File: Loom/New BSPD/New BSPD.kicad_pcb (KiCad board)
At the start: 2 copper layers, 148.6 x 83.8 mm, 62 parts, among them J1 Conn_01x03, J2 Conn_01x03, J3 Conn_01x03, J4 Screw_Terminal_01x02, K1 MCCMA51-S-DC12V-C, Q1 IRLZ44Z, U1 4011, U10 LM2901, U11 4012, U12 74LS573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

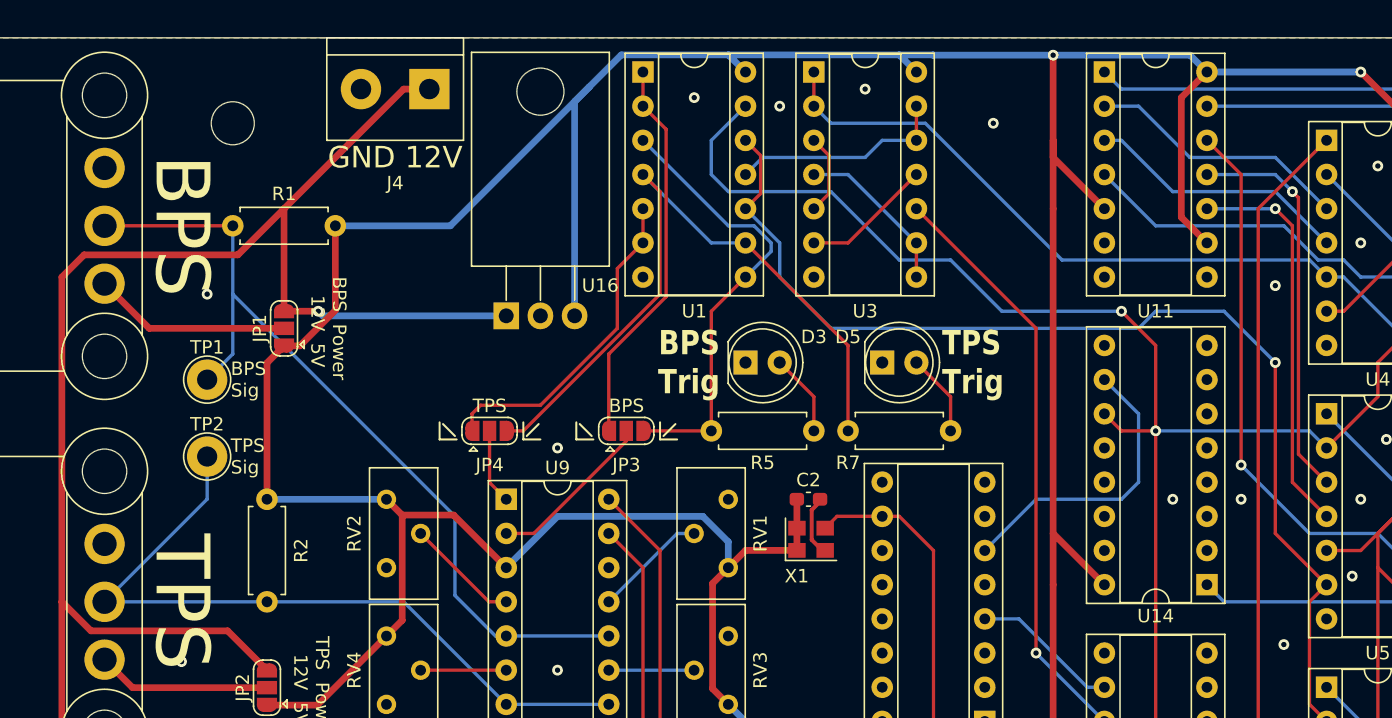
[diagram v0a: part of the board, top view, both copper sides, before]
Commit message: Change BSPD Power connector
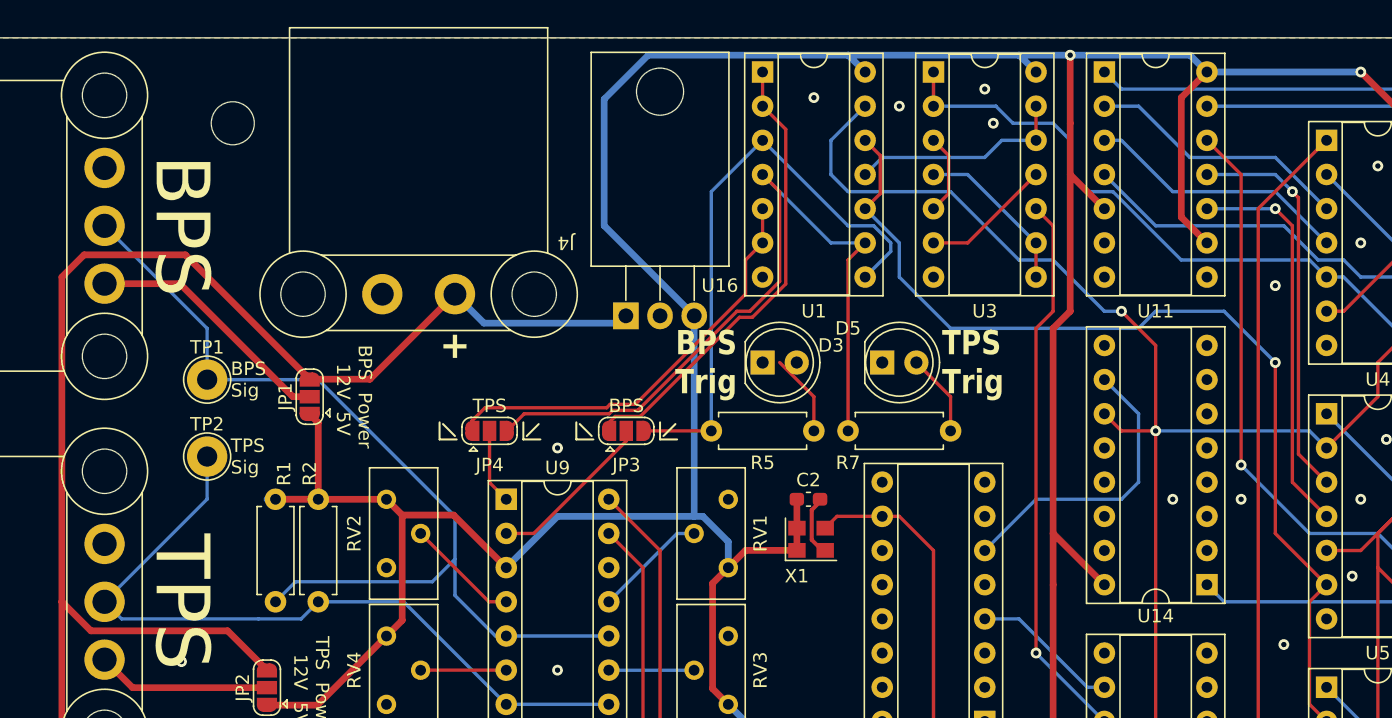
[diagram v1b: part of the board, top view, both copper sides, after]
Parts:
- J4: footprint TerminalBlock:TerminalBlock_bornier-2_P5.08mm -> BSPD_footprints:ATF13-2P-BM03
- moved R1 28.1 mm to (84.5, 64.8), turned to 90 degrees
- moved J4 15.4 mm to (97.8, 41.9)
- moved U1 8.89 mm to (120.7, 25.4)
- moved U16 8.89 mm to (110.5, 43.5)
- moved U3 8.89 mm to (133.3, 25.4)
- moved JP1 5.43 mm to (87.0, 49.5)
- moved R2 3.81 mm to (87.6, 64.8)
- moved D3 1.27 mm to (120.7, 47.0)
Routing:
- net +5V: track 475.2 -> 447.9 mm
- net /BPS_Trig: track 33.5 -> 44.2 mm
- net /System_OK: track 82.0 -> 73.1 mm
- net /State Machine/State_B: track 230.8 -> 221.9 mm
- net Net-(JP4-A): track 24.4 -> 31.8 mm
- net /SM_Ok: track 205.2 -> 197.8 mm
- net +12V: track 153.5 -> 146.3 mm, vias 1 -> 0
- net /BPS_Sig: track 63.7 -> 70.4 mm
- net /TPS_Trig: track 51.8 -> 57.5 mm
- net Net-(JP3-A): track 29.1 -> 34.5 mm
- net /BPS_Power: track 14.7 -> 18.7 mm
- net /State Machine/Timers/Reset_Counting: track 43.9 -> 41.3 mm
- net /TPS_Sig: track 54.6 -> 55.6 mm
- net GND: vias 24 -> 23
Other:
- board text added: "+"
- board text added: "12V GND"
- board text removed: "GND 12V"

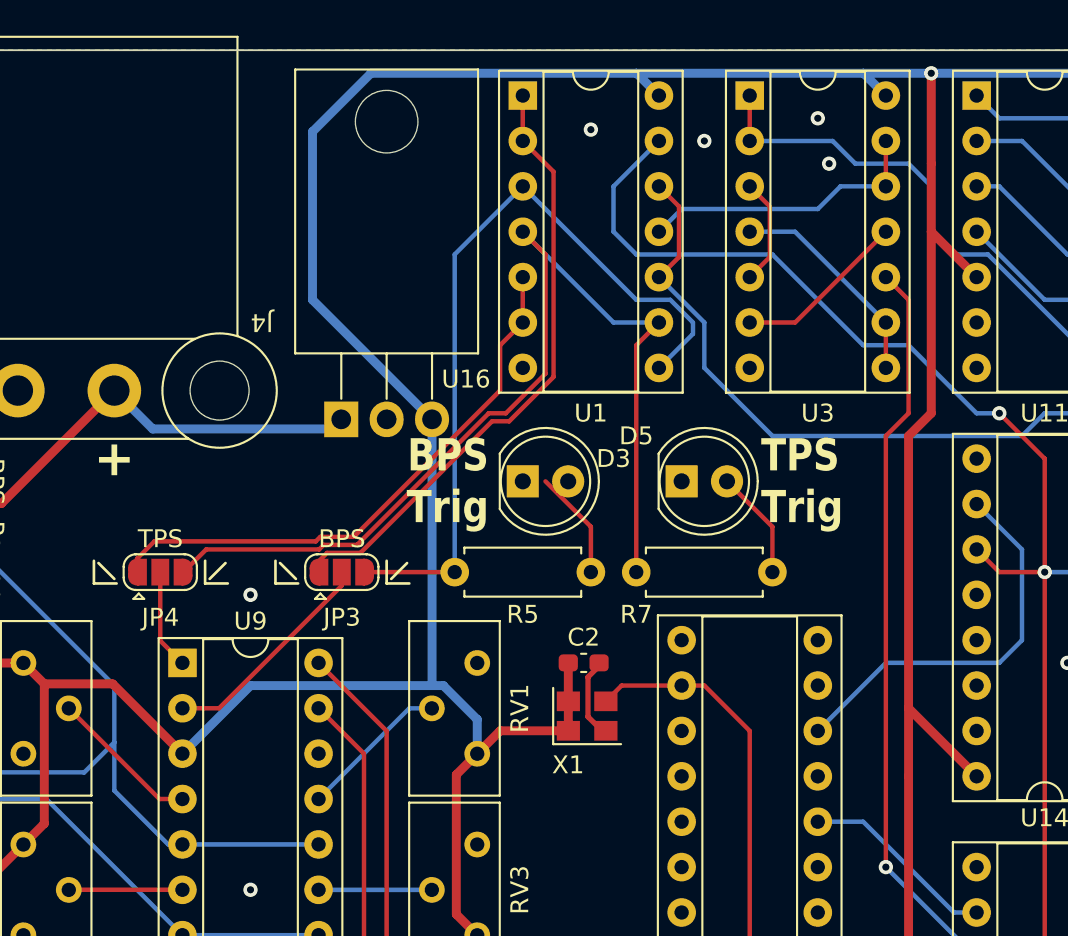
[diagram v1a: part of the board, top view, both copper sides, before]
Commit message: Minor changes to pass DRC
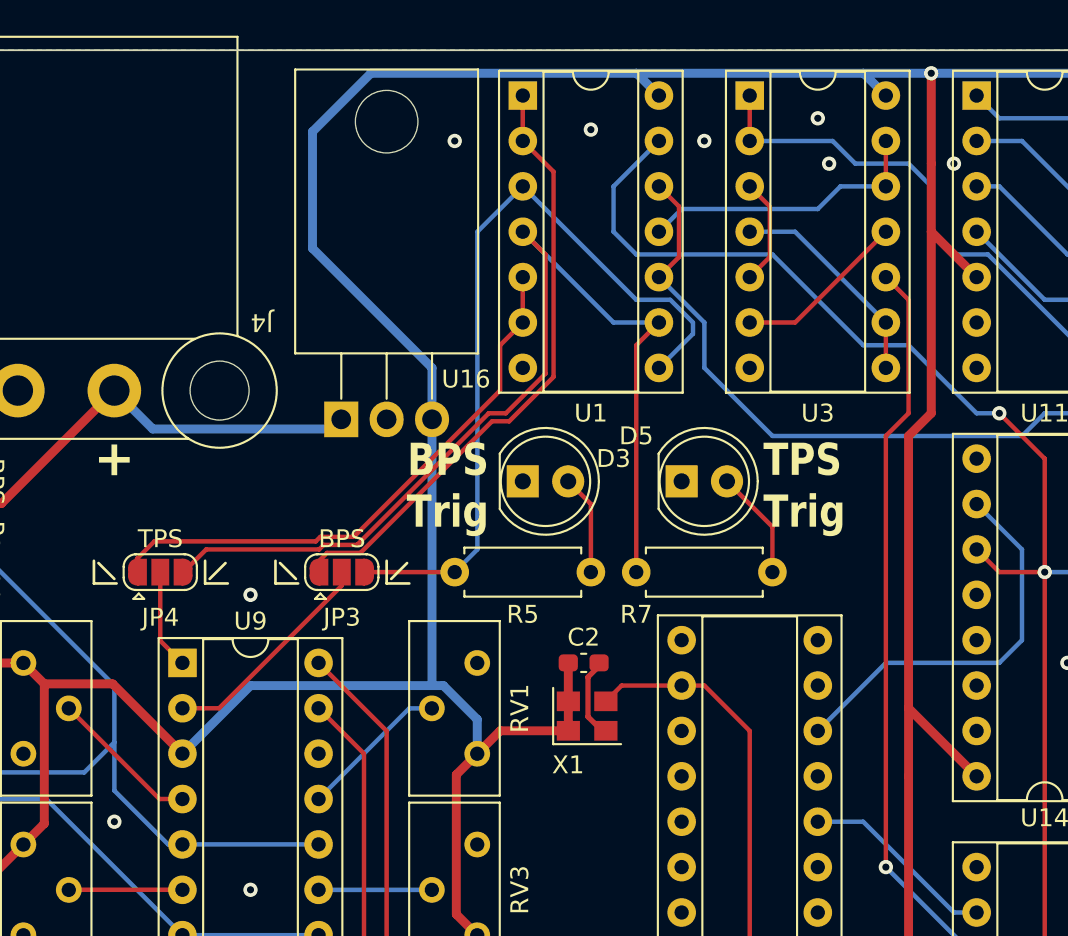
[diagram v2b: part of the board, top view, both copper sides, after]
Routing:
- net Net-(D3-A): track 6.13 -> 5.61 mm
- net GND: vias 23 -> 26
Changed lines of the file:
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@@
     (effects (font (size 1 1) (thickness 0.15)) (justify left))
   )
-  (gr_text "TPS\nTrig" (at 133.985 46.99) (layer "F.SilkS")
+  (gr_text "TPS\nTrig" (at 134.112 47.244) (layer "F.SilkS")
     (effects (font (size 1.8 1.5) (thickness 0.3) bold) (justify left))
   )
@@
     (effects (font (size 2 2) (thickness 0.4) bold))
   )
-  (gr_text "BPS\nTrig" (at 118.745 46.99) (layer "F.SilkS")
+  (gr_text "BPS\nTrig" (at 118.745 47.244) (layer "F.SilkS")
     (effects (font (size 1.8 1.5) (thickness 0.3) bold) (justify right))
   )
@@
   (segment (start 139.72 24.15) (end 139.7 24.15) (width 0.5) (layer "B.Cu") (net 1))
   (segment (start 116.205 58.42) (end 115.57 58.42) (width 0.5) (layer "B.Cu") (net 1))
-  (segment (start 108.88 27.419009) (end 108.88 36.83) (width 0.5) (layer "B.Cu") (net 1))
   (segment (start 115.57 43.52) (end 115.57 58.42) (width 0.5) (layer "B.Cu") (net 1))
   (segment (start 118.1 62.235) (end 118.1 60.315) (width 0.5) (layer "B.Cu") (net 1))
@@
   (segment (start 128.27 25.4) (end 127.02 24.15) (width 0.5) (layer "B.Cu") (net 1))
   (segment (start 184.235 59.605) (end 186.68 59.605) (width 0.5) (layer "B.Cu") (net 1))
+  (segment (start 112.149009 24.15) (end 127 24.15) (width 0.5) (layer "B.Cu") (net 1))
   (segment (start 186.68 59.605) (end 187.875 59.605) (width 0.5) (layer "B.Cu") (net 1))
   (segment (start 127.02 24.15) (end 127 24.15) (width 0.5) (layer "B.Cu") (net 1))
@@
   (segment (start 181.695 41.825) (end 184.235 39.285) (width 0.5) (layer "B.Cu") (net 1))
   (segment (start 195.58 74.85) (end 194.31 76.12) (width 0.5) (layer "B.Cu") (net 1))
+  (segment (start 115.57 40.64) (end 108.88 33.95) (width 0.5) (layer "B.Cu") (net 1))
   (segment (start 118.1 60.315) (end 116.205 58.42) (width 0.5) (layer "B.Cu") (net 1))
   (segment (start 119.365 73.66) (end 118.1 72.395) (width 0.5) (layer "B.Cu") (net 1))
@@
   (segment (start 139.7 24.15) (end 127 24.15) (width 0.5) (layer "B.Cu") (net 1))
   (segment (start 105.41 58.42) (end 101.6 62.23) (width 0.5) (layer "B.Cu") (net 1))
-  (segment (start 127 24.15) (end 112.149009 24.15) (width 0.5) (layer "B.Cu") (net 1))
   (segment (start 140.97 25.4) (end 139.72 24.15) (width 0.5) (layer "B.Cu") (net 1))
   (segment (start 196.77 81.2) (end 196.85 81.28) (width 0.5) (layer "B.Cu") (net 1))
-  (segment (start 115.57 43.52) (end 108.88 36.83) (width 0.5) (layer "B.Cu") (net 1))
   (segment (start 187.875 59.605) (end 195.58 67.31) (width 0.5) (layer "B.Cu") (net 1))
   (segment (start 196.85 76.12) (end 196.85 81.28) (width 0.5) (layer "B.Cu") (net 1))
@@
   (segment (start 195.58 67.31) (end 195.58 74.85) (width 0.5) (layer "B.Cu") (net 1))
   (segment (start 179.06 41.825) (end 181.695 41.825) (width 0.5) (layer "B.Cu") (net 1))
-  (segment (start 112.149009 24.15) (end 108.88 27.419009) (width 0.5) (layer "B.Cu") (net 1))
   (segment (start 153.67 25.4) (end 165.1 25.4) (width 0.5) (layer "B.Cu") (net 1))
   (segment (start 175.335 38.1) (end 175.26 38.1) (width 0.5) (layer "B.Cu") (net 1))
+  (segment (start 108.88 33.95) (end 108.88 27.419009) (width 0.5) (layer "B.Cu") (net 1))
   (segment (start 179.06 62.145) (end 181.695 62.145) (width 0.5) (layer "B.Cu") (net 1))
   (segment (start 129.54 73.66) (end 119.365 73.66) (width 0.5) (layer "B.Cu") (net 1))
   (segment (start 195.58 74.85) (end 196.85 76.12) (width 0.5) (layer "B.Cu") (net 1))
+  (segment (start 115.57 43.52) (end 115.57 40.64) (width 0.5) (layer "B.Cu") (net 1))
   (segment (start 179.06 41.825) (end 175.335 38.1) (width 0.5) (layer "B.Cu") (net 1))
   (segment (start 115.57 58.42) (end 105.41 58.42) (width 0.5) (layer "B.Cu") (net 1))
@@
   (segment (start 184.235 39.285) (end 186.68 39.285) (width 0.5) (layer "B.Cu") (net 1))
   (segment (start 181.695 62.145) (end 184.235 59.605) (width 0.5) (layer "B.Cu") (net 1))
+  (segment (start 108.88 27.419009) (end 112.149009 24.15) (width 0.5) (layer "B.Cu") (net 1))
   (segment (start 195.58 87.55) (end 196.85 86.28) (width 0.25) (layer "B.Cu") (net 2))
   (segment (start 191.77 87.55) (end 195.58 87.55) (width 0.25) (layer "B.Cu") (net 2))
@@
   (via (at 159.385 67.945) (size 0.8) (drill 0.4) (layers "F.Cu" "B.Cu") (free) (net 5))
   (via (at 164.465 62.865) (size 0.8) (drill 0.4) (layers "F.Cu" "B.Cu") (free) (net 5))
+  (via (at 116.84 27.94) (size 0.8) (drill 0.4) (layers "F.Cu" "B.Cu") (free) (net 5))
   (via (at 167.005 52.705) (size 0.8) (drill 0.4) (layers "F.Cu" "B.Cu") (free) (net 5))
   (via (at 128.27 96.52) (size 0.8) (drill 0.4) (layers "F.Cu" "B.Cu") (free) (net 5))
+  (via (at 144.78 29.21) (size 0.8) (drill 0.4) (layers "F.Cu" "B.Cu") (free) (net 5))
   (via (at 137.795 29.21) (size 0.8) (drill 0.4) (layers "F.Cu" "B.Cu") (free) (net 5))
   (via (at 137.16 26.67) (size 0.8) (drill 0.4) (layers "F.Cu" "B.Cu") (free) (net 5))
   (via (at 130.81 27.94) (size 0.8) (drill 0.4) (layers "F.Cu" "B.Cu") (free) (net 5))
   (via (at 105.41 69.85) (size 0.8) (drill 0.4) (layers "F.Cu" "B.Cu") (free) (net 5))
+  (via (at 97.79 66.04) (size 0.8) (drill 0.4) (layers "F.Cu" "B.Cu") (free) (net 5))
   (via (at 165.1 38.1) (size 0.8) (drill 0.4) (layers "F.Cu" "B.Cu") (free) (net 5))
   (segment (start 151.13 100.33) (end 151.13 102.87) (width 0.25) (layer "F.Cu") (net 6))
   (segment (start 148.59 97.79) (end 151.13 100.33) (width 0.25) (layer "F.Cu") (net 6))
-  (segment (start 124.46 49.53) (end 124.46 52.07) (width 0.25) (layer "F.Cu") (net 7))
-  (segment (start 121.92 46.99) (end 124.46 49.53) (width 0.25) (layer "F.Cu") (net 7))
+  (segment (start 124.46 48.26) (end 123.19 46.99) (width 0.25) (layer "F.Cu") (net 7))
+  (segment (start 124.46 52.07) (end 124.46 48.26) (width 0.25) (layer "F.Cu") (net 7))
   (segment (start 161.29 100.33) (end 161.29 102.87) (width 0.25) (layer "F.Cu") (net 8))
   (segment (start 158.75 97.79) (end 161.29 100.33) (width 0.25) (layer "F.Cu") (net 8))
@@
   (segment (start 120.65 30.48) (end 127 36.83) (width 0.25) (layer "B.Cu") (net 19))
   (segment (start 130.175 38.101396) (end 130.175 38.735) (width 0.25) (layer "B.Cu") (net 19))
-  (segment (start 116.84 34.29) (end 116.84 52.07) (width 0.25) (layer "B.Cu") (net 19))
+  (segment (start 120.65 30.48) (end 118.11 33.02) (width 0.25) (layer "B.Cu") (net 19))
+  (segment (start 118.11 50.8) (end 116.84 52.07) (width 0.25) (layer "B.Cu") (net 19))
   (segment (start 130.175 38.735) (end 128.27 40.64) (width 0.25) (layer "B.Cu") (net 19))
   (segment (start 128.903604 36.83) (end 130.175 38.101396) (width 0.25) (layer "B.Cu") (net 19))
-  (segment (start 120.65 30.48) (end 116.84 34.29) (width 0.25) (layer "B.Cu") (net 19))
+  (segment (start 118.11 33.02) (end 118.11 50.8) (width 0.25) (layer "B.Cu") (net 19))
   (segment (start 109.322208 50.095) (end 111.192208 50.095) (width 0.25) (layer "F.Cu") (net 20))
   (segment (start 119.38 41.907208) (end 119.38 39.37) (width 0.25) (layer "F.Cu") (net 20))

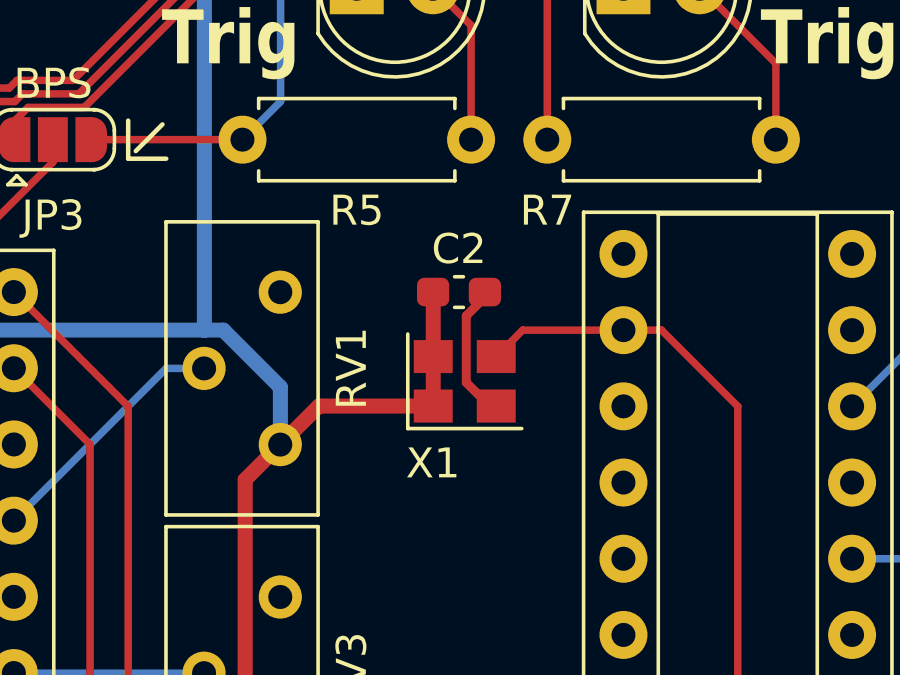
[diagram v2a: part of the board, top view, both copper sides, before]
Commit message: Fix BSPD Crystal Footprint
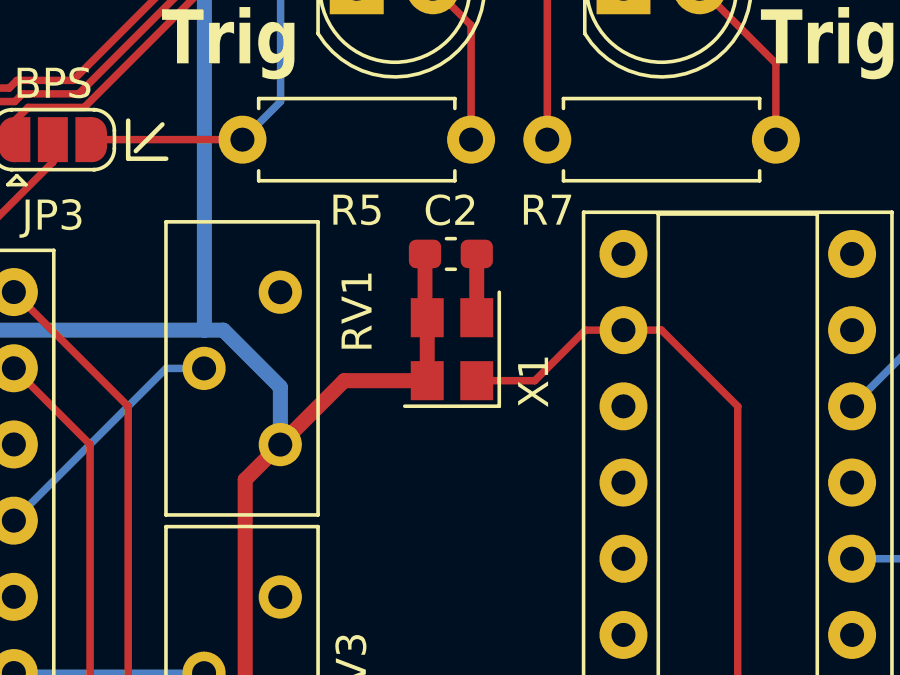
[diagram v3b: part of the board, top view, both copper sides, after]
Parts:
- moved C2 1.30 mm to (123.8, 55.9)
- moved X1 1.15 mm to (123.8, 59.1), turned to 90 degrees
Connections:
- X1 pad 1: +5V -> /CLK
- X1 pad 3: /CLK -> +5V
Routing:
- net GND: track 4.60 -> 2.12 mm
- net /CLK: track 29.6 -> 30.6 mm
- net +5V: track 447.9 -> 448.5 mm
